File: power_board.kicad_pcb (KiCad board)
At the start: 2 copper layers, 141 x 90 mm, 170 parts, among them CON1 MICROUSB, J1 Conn_02x03_Odd_Even, J10 Conn_01x02, J11 Conn_01x02, J12 Conn_01x02, J13 Conn_01x02, J14 Conn_01x02, J15 Conn_01x02, J16 Conn_01x02, J17 Conn_01x02, J18 Conn_01x02, J19 Conn_01x02, J2 Conn_01x01, J20 Conn_01x02, J21 Conn_01x03, J22 Conn_01x03, J23 Conn_01x03, J24 Conn_01x03, J25 Conn_01x03, J26 Conn_01x02, J27 Conn_01x02, J28 Conn_01x02, J29 Conn_01x02, J3 Conn_01x01, J30 Conn_01x02, J31 Conn_01x02, J32 Conn_01x02, J33 Conn_01x02, J4 Conn_01x01, J5 ATX-24, J6 Conn_01x02, J7 Conn_01x02, J8 Conn_01x02, J9 Conn_01x02, K1 RELAY_1RT, K2 RELAY_1RT, K3 RELAY_1RT, K4 RELAY_1RT, K5 RELAY_1RT, Q1 MMBT4401-7-F, Q10 MMBT4401-7-F, Q11 SI7113ADN-T1-GE3, Q12 MMBT4401-7-F, Q13 MMBT4401-7-F, Q14 MMBT4401-7-F, Q15 SI7113ADN-T1-GE3, Q16 SI7113ADN-T1-GE3, Q17 SI7113ADN-T1-GE3, Q18 MMBT4401-7-F, Q19 MMBT4401-7-F, Q2 MMBT4401-7-F, Q20 SI7113ADN-T1-GE3, Q21 SI7113ADN-T1-GE3, Q3 MMBT4401-7-F, Q4 SI7113ADN-T1-GE3, Q5 SI7113ADN-T1-GE3, Q6 MMBT4401-7-F, Q7 MMBT4401-7-F, Q8 SI7113ADN-T1-GE3, Q9 SI7113ADN-T1-GE3, SW1 SW_Push, U1 PCA9555PW, U10 DRV8801PWP, U11 DRV8801PWP, U12 DRV8801PWP, U2 ATMEGA328P-AU, U3 PCA9555PW, U4 FT232RL, U5 DRV8801PWP, U6 DRV8801PWP, U7 DRV8801PWP, U8 DRV8801PWP, U9 DRV8801PWP, Y1 Crystal

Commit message: Routing.
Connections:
- U1 pad 10: /MTR1_PH -> /MTR1_SL
- U1 pad 11: /MTR1_SL -> /MTR1_EN
- U1 pad 16: /MTR3_PH -> /MTR3_SL
- U1 pad 17: /MTR3_SL -> /MTR3_PH
- U1 pad 19: /MTR2_PH -> /MTR2_SL
- U1 pad 20: /MTR2_SL -> /MTR2_PH
- U1 pad 9: /MTR1_EN -> /MTR1_PH
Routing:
- net +12V: track 338.6 -> 591.8 mm, vias 1 -> 9
- net /MTR1_EN: track 0.00 -> 49.7 mm
- net /MTR1_SL: track 0.00 -> 48.6 mm
- net /MTR1_PH: track 0.00 -> 47.2 mm
- net Net-(J33-Pad1): track 0.00 -> 14.9 mm
- net Net-(J28-Pad1): track 0.00 -> 14.9 mm
- net Net-(J27-Pad1): track 0.00 -> 14.9 mm
- net Net-(J32-Pad1): track 0.00 -> 14.9 mm
- net Net-(J30-Pad1): track 0.00 -> 14.9 mm
- net Net-(J26-Pad1): track 0.00 -> 14.9 mm
- net Net-(J31-Pad1): track 0.00 -> 14.9 mm
- net Net-(J29-Pad1): track 0.00 -> 14.9 mm
- net Net-(J33-Pad2): track 0.00 -> 11.3 mm
- net Net-(J31-Pad2): track 0.00 -> 11.3 mm
- net Net-(J29-Pad2): track 0.00 -> 11.3 mm
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
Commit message: New driver arrangement
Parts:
- moved R4 9.23 mm to (146.4, 94.1), turned to 90 degrees
- moved C17 9.04 mm to (82.9, 74.0), turned to 0 degrees
- moved C19 9.04 mm to (97.9, 74.0), turned to 0 degrees
- moved C21 9.04 mm to (112.9, 74.0), turned to 0 degrees
- moved C29 9.04 mm to (127.9, 74.0), turned to 0 degrees
- moved C31 9.04 mm to (142.9, 74.0), turned to 0 degrees
- moved C33 9.04 mm to (157.9, 74.0), turned to 0 degrees
- moved C39 9.04 mm to (172.9, 74.0), turned to 0 degrees
- moved C41 9.04 mm to (187.9, 74.0), turned to 0 degrees
- moved C23 8.52 mm to (135.6, 71.5), turned to 180 degrees
- moved C24 8.52 mm to (150.6, 71.5), turned to 180 degrees
- moved C25 8.52 mm to (165.6, 71.5), turned to 180 degrees
- moved C35 8.52 mm to (180.6, 71.5), turned to 180 degrees
- moved C36 8.52 mm to (195.6, 71.5), turned to 180 degrees
- moved C11 8.52 mm to (90.5, 71.5), turned to 180 degrees
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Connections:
- U3 pad 13: /MTR8_PH -> /MTR8_SL
- U3 pad 14: /MTR8_SL -> /MTR8_PH
- U3 pad 16: /MTR7_PH -> /MTR7_SL
- U3 pad 17: /MTR7_SL -> /MTR7_PH
- U3 pad 19: /MTR6_PH -> /MTR6_SL
- U3 pad 20: /MTR6_SL -> /MTR6_PH
- U3 pad 4: /MTR4_EN -> /MTR4_PH
- U3 pad 5: /MTR4_PH -> /MTR4_SL
- U3 pad 6: /MTR4_SL -> /MTR4_EN
- U3 pad 7: /MTR5_EN -> /MTR5_PH
- U3 pad 8: /MTR5_PH -> /MTR5_SL
- U3 pad 9: /MTR5_SL -> /MTR5_EN
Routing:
- net +12V: track 591.8 -> 480.4 mm
- net /MTR5_PH: track 0.00 -> 36.6 mm
- net /MTR4_PH: track 0.00 -> 31.7 mm
- net /MTR4_SL: track 0.00 -> 31.5 mm
- net /MTR4_EN: track 0.00 -> 31.4 mm
- net /MTR2_PH: track 0.00 -> 22.1 mm
- net /MTR5_SL: track 0.00 -> 22.0 mm
- net /MTR2_SL: track 0.00 -> 21.8 mm
- net /MTR2_EN: track 0.00 -> 21.8 mm
- net /MTR3_EN: track 0.00 -> 19.5 mm
- net /MTR3_SL: track 0.00 -> 19.5 mm
- net /MTR3_PH: track 0.00 -> 19.2 mm
- net Net-(J33-Pad1): track 14.9 -> 27.8 mm
- net Net-(J32-Pad1): track 14.9 -> 27.2 mm
- net Net-(J26-Pad1): track 14.9 -> 27.2 mm
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
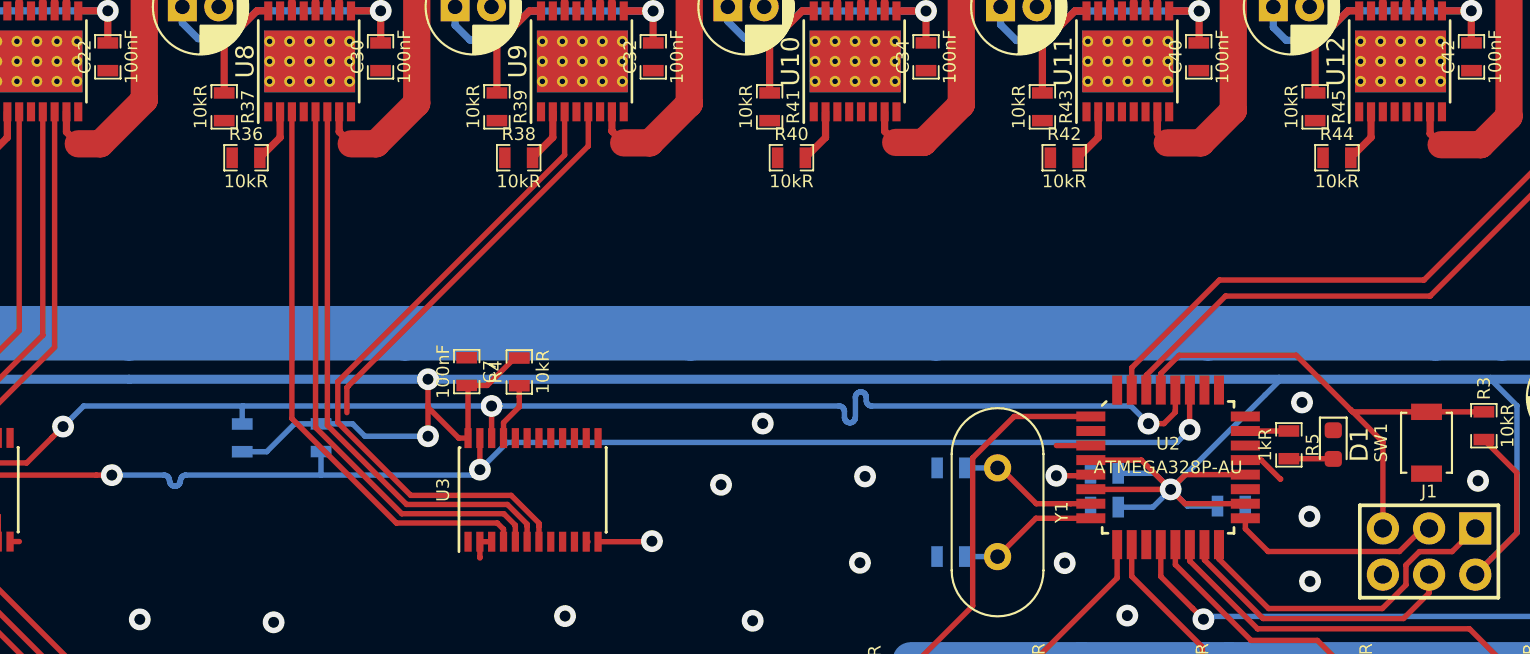
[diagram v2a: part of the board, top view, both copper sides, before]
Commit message: Driver control routed
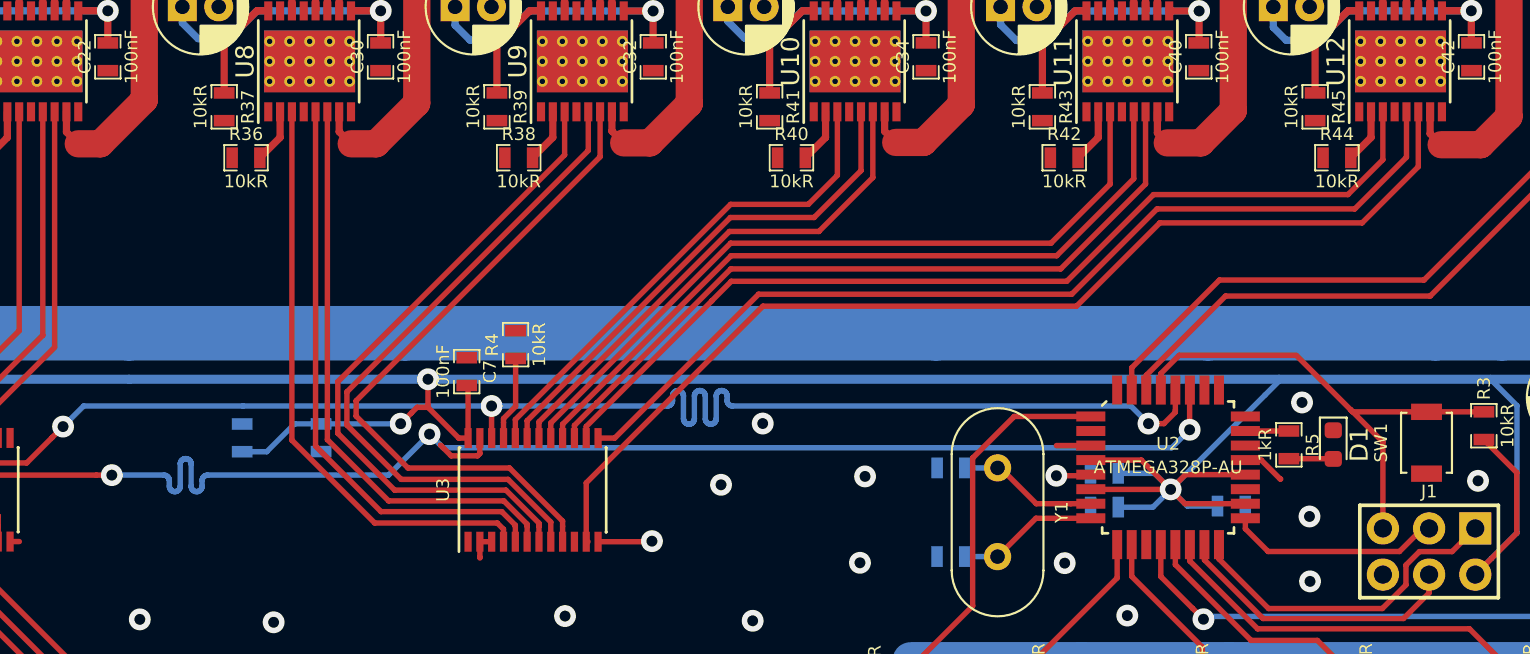
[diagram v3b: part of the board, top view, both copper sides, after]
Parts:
- moved R4 1.51 mm to (146.2, 92.6)
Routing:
- net /MTR8_EN: track 0.10 -> 59.3 mm
- net /MTR8_SL: track 0.00 -> 53.4 mm
- net /MTR8_PH: track 0.00 -> 53.2 mm
- net /MTR7_EN: track 0.00 -> 41.6 mm
- net /MTR7_SL: track 0.00 -> 41.4 mm
- net /MTR7_PH: track 0.00 -> 41.0 mm
- net /MTR5_EN: track 0.00 -> 37.2 mm
- net /MTR6_EN: track 0.00 -> 28.4 mm
- net /MTR6_SL: track 0.00 -> 28.2 mm
- net /MTR6_PH: track 0.00 -> 27.8 mm
- net /MTR5_SL: track 22.0 -> 37.2 mm
- net /+5V_SB: track 195.4 -> 190.4 mm
- net /SDA: track 80.1 -> 84.5 mm
- net /SCL: track 79.6 -> 83.5 mm
- net Net-(R4-Pad1): track 3.24 -> 4.65 mm
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
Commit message: Finished connections
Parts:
- moved R40 0.60 mm to (162.0, 82.3)
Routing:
- net +5V: track 183.7 -> 507.2 mm, vias 0 -> 8
- net GND: track 23.8 -> 183.9 mm, vias 58 -> 105
- net +12V: track 480.4 -> 633.8 mm
- net /+5V_SB: track 190.4 -> 195.2 mm
- net /SDA: track 84.5 -> 86.6 mm
- net /SCL: track 83.5 -> 84.5 mm
- net /MTR5_EN: track 37.2 -> 36.5 mm
- net /MTR6_PH: track 27.8 -> 28.3 mm

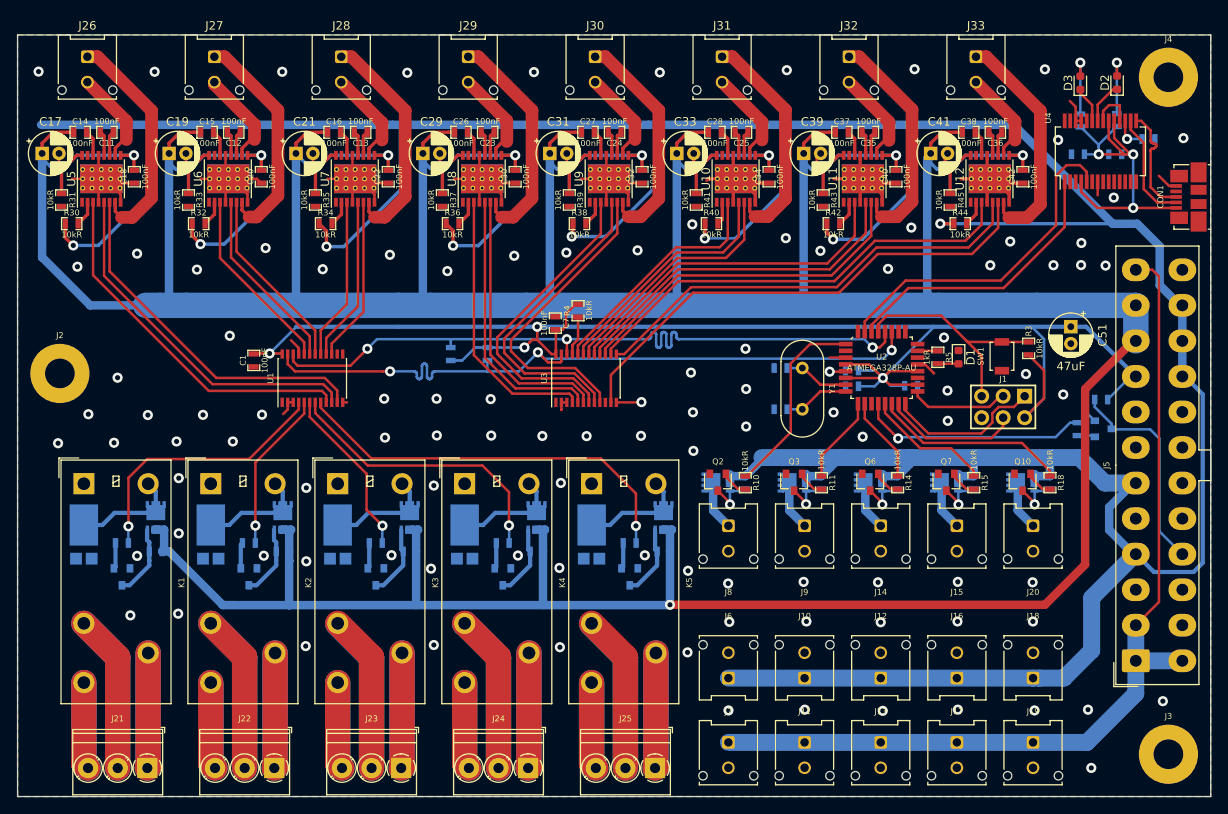
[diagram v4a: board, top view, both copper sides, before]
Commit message: Finished silkscreen.
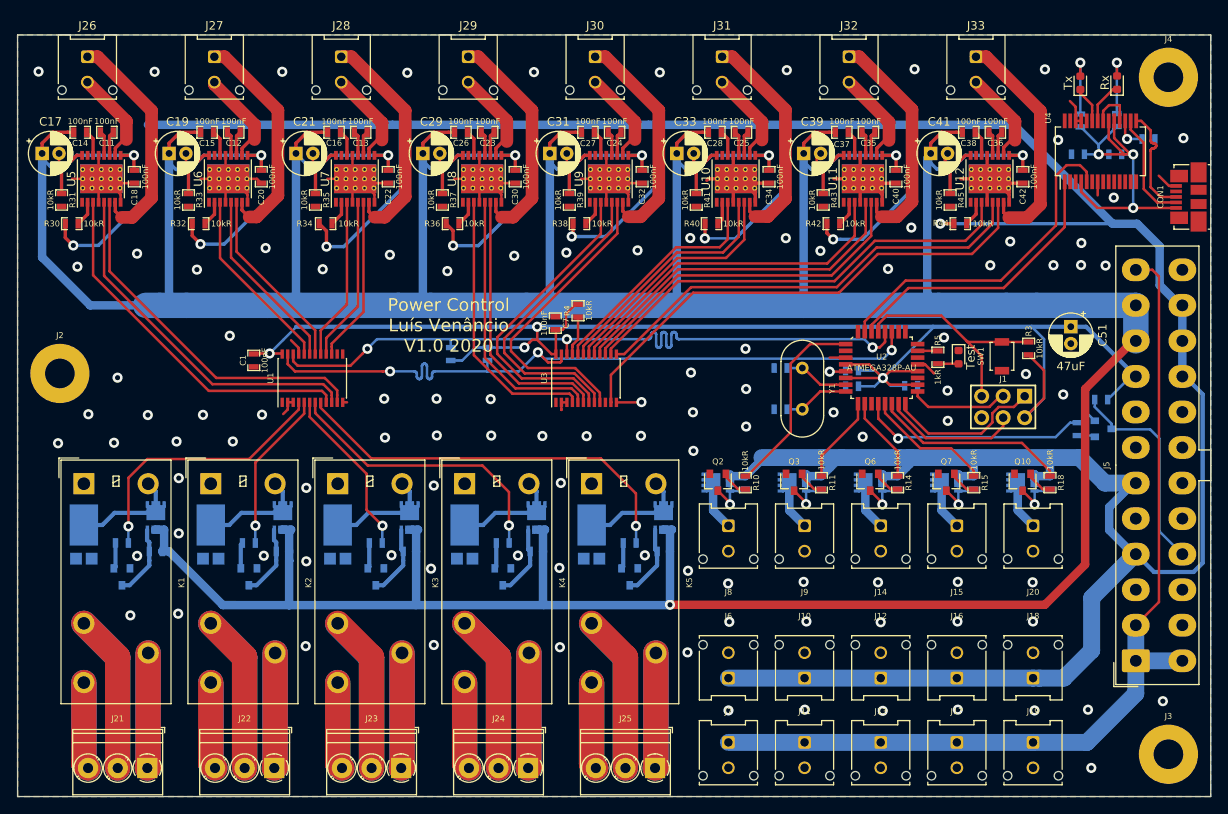
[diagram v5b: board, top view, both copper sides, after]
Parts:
- renumbered D2 to Rx, D1 to Test, D3 to Tx
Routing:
- net +5V: track 507.2 -> 494.6 mm
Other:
- board text added: "Power Control Luís Venâncio V1.0 2020"

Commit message: Improvements
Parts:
- moved D4 10.6 mm to (90.7, 108.9), turned to 180 degrees
- moved D5 10.6 mm to (105.7, 108.9), turned to 180 degrees
- moved D6 10.6 mm to (120.7, 108.9), turned to 180 degrees
- moved D7 10.6 mm to (135.7, 108.9), turned to 180 degrees
- moved D8 10.6 mm to (150.7, 108.9), turned to 180 degrees
- moved C9 4.87 mm to (209.7, 76.2), turned to 180 degrees
- moved Q12 3.05 mm to (91.8, 121.0), turned to 0 degrees
- moved Q13 3.05 mm to (106.8, 121.0), turned to 0 degrees
- moved Q14 3.05 mm to (121.8, 121.0), turned to 0 degrees
- moved Q18 3.05 mm to (136.8, 121.0), turned to 0 degrees
- moved Q19 3.05 mm to (151.8, 121.0), turned to 0 degrees
- moved R20 2.23 mm to (91.9, 117.8), turned to 270 degrees
- moved R21 2.23 mm to (106.9, 117.8), turned to 270 degrees
- moved R22 2.23 mm to (121.9, 117.8), turned to 270 degrees
- moved R26 2.23 mm to (136.9, 117.8), turned to 270 degrees
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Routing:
- net +12V: track 633.8 -> 583.3 mm
- net GND: track 183.9 -> 218.6 mm, vias 105 -> 91
- net Net-(Q13-PadC): track 8.54 -> 3.78 mm
- net Net-(Q12-PadC): track 8.54 -> 3.78 mm
- net Net-(Q14-PadC): track 8.53 -> 3.78 mm
- net Net-(Q19-PadC): track 8.53 -> 3.78 mm
- net Net-(Q18-PadC): track 8.53 -> 3.78 mm
- net /RLY3_EN: track 20.2 -> 16.7 mm
- net /RLY4_EN: track 34.1 -> 30.6 mm
- net /RLY5_EN: track 47.9 -> 44.5 mm
- net /RLY2_EN: track 19.0 -> 16.6 mm
- net /RLY1_EN: track 32.0 -> 29.8 mm
- net Net-(D7-Pad1): track 12.9 -> 10.7 mm
- net Net-(D6-Pad1): track 12.9 -> 10.7 mm
- net Net-(D5-Pad1): track 12.9 -> 10.8 mm
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- added copper zone on F.Cu, net Net-(J33-Pad1)

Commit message: Small changes and added labels
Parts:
- K1, K2, K3, K4, K5: value RELAY_1RT -> lsts-devices:RELAY_1RT
- renumbered Test to D1, Rx to D2, Tx to D3
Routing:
- net GND: vias 91 -> 94

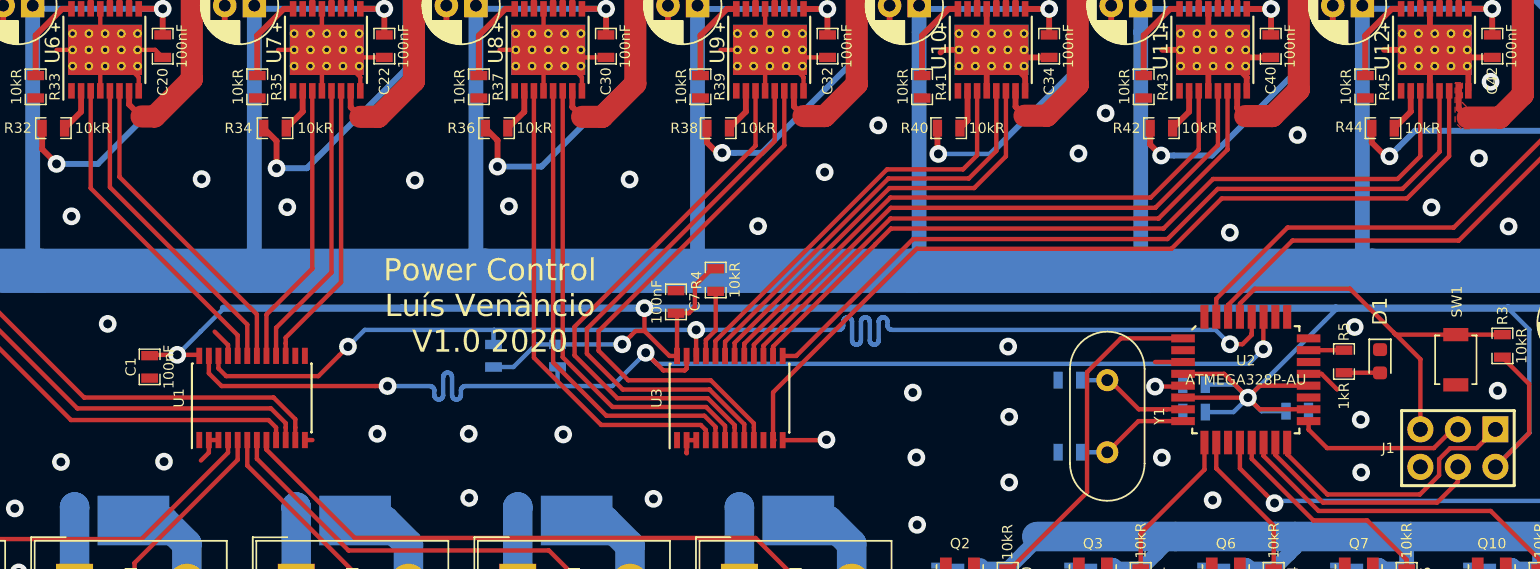
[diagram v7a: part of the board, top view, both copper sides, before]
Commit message: Removed PCA9555 and added PCA9685
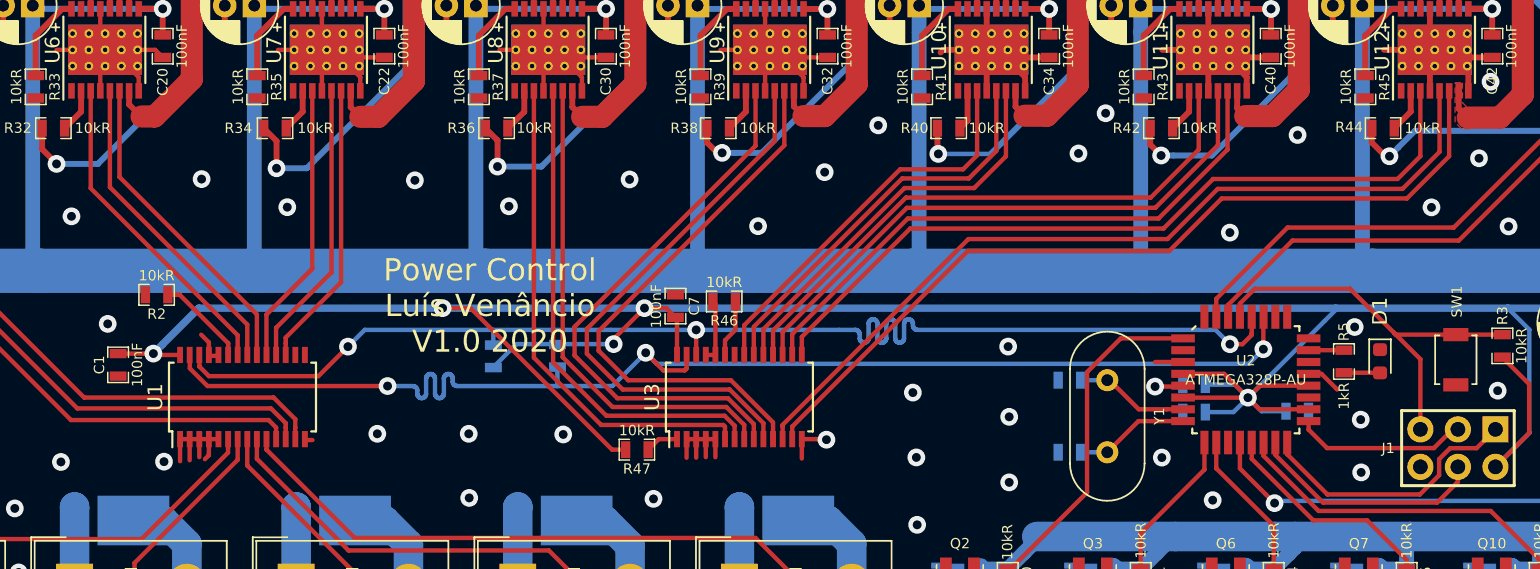
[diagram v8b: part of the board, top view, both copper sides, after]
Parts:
- added R46: 10kR, lsts-passives:R_0603, F.Cu at (146.8, 94.0)
- added R47: 10kR, lsts-passives:R_0603, F.Cu at (140.9, 104.1)
- R2: moved to F.Cu
- R4: moved to B.Cu
- U1, U3: value PCA9555PW -> PCA9685PW; footprint Package_SO:TSSOP-24_4.4x7.8mm_P0.65mm -> Package_SO:TSSOP-28_4.4x9.7mm_P0.65mm
- moved R2 27.5 mm to (108.4, 93.6), turned to 180 degrees
- moved R4 11.9 mm to (135.5, 97.7)
- moved C1 2.14 mm to (105.8, 98.3)
- moved U1 0.65 mm to (114.2, 100.5)
- moved U3 0.65 mm to (147.8, 100.5)
- moved C7 0.28 mm to (143.5, 94.3)
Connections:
- R2 pad 1: /SDA -> Net-(R2-Pad1)
- R2 pad 2: /+5V_SB -> GND
- R4 pad 1: Net-(R4-Pad1) -> /SDA
- U1 pad 1: Net-(U1-Pad1) -> GND
- U1 pad 10: /MTR1_SL -> /RLY5_EN
- U1 pad 11: /MTR1_EN -> /MTR1_PH
- U1 pad 12: GND -> /MTR1_SL
- U1 pad 13: Net-(U1-Pad13) -> /MTR1_EN
- U1 pad 14: Net-(U1-Pad14) -> GND
- U1 pad 15: /MTR3_EN -> Net-(U1-Pad15)
- U1 pad 16: /MTR3_SL -> Net-(U1-Pad16)
- U1 pad 17: /MTR3_PH -> /MTR3_EN
- U1 pad 18: /MTR2_EN -> /MTR3_SL
- U1 pad 19: /MTR2_SL -> /MTR3_PH
- U1 pad 20: /MTR2_PH -> /MTR2_EN
- U1 pad 21: GND -> /MTR2_SL
- U1 pad 22: /SCL -> /MTR2_PH
- U1 pad 23: /SDA -> Net-(R2-Pad1)
- U1 pad 24: /+5V_SB -> GND
- U1 pad 4: /RLY1_EN -> GND
- U1 pad 5: /RLY2_EN -> GND
- U1 pad 6: /RLY3_EN -> /RLY1_EN
- U1 pad 7: /RLY4_EN -> /RLY2_EN
- U1 pad 8: /RLY5_EN -> /RLY3_EN
- U1 pad 9: /MTR1_PH -> /RLY4_EN
- U3 pad 10: Net-(U3-Pad10) -> /MTR5_SL
- U3 pad 11: /MTR8_EN -> /MTR5_EN
- U3 pad 12: GND -> /MTR8_SL
- U3 pad 13: /MTR8_SL -> /MTR8_EN
- U3 pad 14: /MTR8_PH -> GND
- U3 pad 15: /MTR7_EN -> /MTR8_PH
- U3 pad 16: /MTR7_SL -> /MTR7_EN
- U3 pad 17: /MTR7_PH -> /MTR7_SL
- U3 pad 18: /MTR6_EN -> /MTR7_PH
- U3 pad 19: /MTR6_SL -> /MTR6_EN
- U3 pad 20: /MTR6_PH -> /MTR6_SL
- U3 pad 21: Net-(R4-Pad1) -> /MTR6_PH
- U3 pad 22: /SCL -> Net-(U3-Pad22)
- U3 pad 23: /SDA -> Net-(R46-Pad1)
- U3 pad 24: /+5V_SB -> GND
- U3 pad 4: /MTR4_PH -> GND
- U3 pad 5: /MTR4_SL -> GND
- U3 pad 6: /MTR4_EN -> /MTR4_PH
- U3 pad 7: /MTR5_PH -> /MTR4_SL
- U3 pad 8: /MTR5_SL -> /MTR4_EN
- U3 pad 9: /MTR5_EN -> /MTR5_PH
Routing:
- net GND: track 218.6 -> 234.5 mm
- net /+5V_SB: track 195.2 -> 207.5 mm, vias 4 -> 5
- net Net-(R2-Pad1): track 0.00 -> 6.30 mm
- net Net-(R4-Pad1): track 4.65 -> 0.00 mm
- net Net-(R46-Pad1): track 0.00 -> 3.91 mm
- net /MTR8_SL: track 54.3 -> 57.2 mm
- net /MTR8_EN: track 60.1 -> 57.3 mm
- net Net-(R47-Pad1): track 0.00 -> 2.25 mm
- net /SDA: track 86.6 -> 88.6 mm
- net /MTR8_PH: track 54.2 -> 52.6 mm
- net /MTR7_EN: track 41.6 -> 40.0 mm
- net /MTR7_SL: track 41.4 -> 39.9 mm
- net /MTR7_PH: track 41.0 -> 39.5 mm
- net /MTR6_EN: track 28.9 -> 27.4 mm
- net /MTR6_SL: track 28.7 -> 27.3 mm
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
